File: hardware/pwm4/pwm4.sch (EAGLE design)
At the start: 79 parts, among them IC1 BSP75, IC2 PCA82C250SMD, IC3 BSP75, IC4 78L05SMD, IC6 BSP75, IC7 BSP75, Q1 18M432

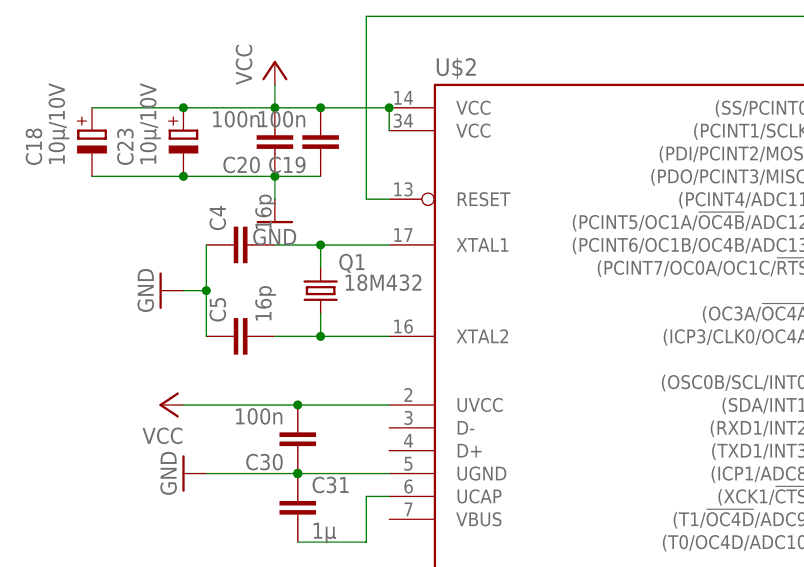
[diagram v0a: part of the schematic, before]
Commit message: changed crystal frequency
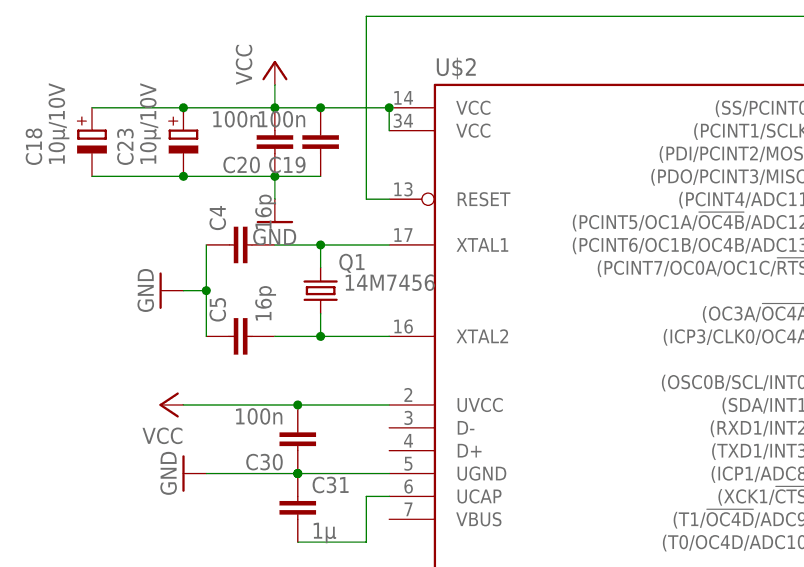
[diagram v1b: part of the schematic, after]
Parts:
- Q1: value 18M432 -> 14M7456
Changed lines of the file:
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@@
 <part name="C2" library="rcl" deviceset="CPOL-EU" device="A/3216-18W" value="10µ/10V"/>
 <part name="GND1" library="supply1" deviceset="GND" device=""/>
-<part name="Q1" library="crystal" deviceset="CRYSTAL" device="SM49" value="18M432"/>
+<part name="Q1" library="crystal" deviceset="CRYSTAL" device="SM49" value="14M7456"/>
 <part name="GND6" library="supply1" deviceset="GND" device=""/>
 <part name="C4" library="resistor" deviceset="C-EU" device="C0603" value="16p"/>

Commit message: optocoupler input and output resistor change
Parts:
- C22, C26, C6, C8: value 2n2 -> n.b.
- R1, R2, R3, R6: value 680 -> 1k2
- R10, R11, R7, R9: value 1k -> 2k2
- renumbered U$10 to BUS, U$5 to PWM0, U$6 to PWM1, U$7 to PWM2, U$8 to PWM3, U$9 to 24V
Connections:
- net N$33 renamed PWM1
- net N$34 renamed PWM2
- net N$35 renamed PWM0
- net N$5 renamed MOSI
- net N$6 renamed MISO
- net N$7 renamed SCK
- net N$8 renamed PWM3
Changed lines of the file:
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@@
 <part name="D15" library="diode" deviceset="SCHOTTKY-DIODE" device="SMD" value="SS24"/>
 <part name="U$4" library="mylib" deviceset="TCMT4100" device=""/>
-<part name="R1" library="resistor" deviceset="R-EU_" device="R0603" value="680"/>
-<part name="R2" library="resistor" deviceset="R-EU_" device="R0603" value="680"/>
-<part name="R3" library="resistor" deviceset="R-EU_" device="R0603" value="680"/>
-<part name="R6" library="resistor" deviceset="R-EU_" device="R0603" value="680"/>
+<part name="R1" library="resistor" deviceset="R-EU_" device="R0603" value="1k2"/>
+<part name="R2" library="resistor" deviceset="R-EU_" device="R0603" value="1k2"/>
+<part name="R3" library="resistor" deviceset="R-EU_" device="R0603" value="1k2"/>
+<part name="R6" library="resistor" deviceset="R-EU_" device="R0603" value="1k2"/>
 <part name="GND14" library="supply1" deviceset="GND" device=""/>
 <part name="GND15" library="supply1" deviceset="GND" device=""/>
@@
 <part name="VCC4" library="supply1" deviceset="VCCIO" device=""/>
 <part name="VCC5" library="supply1" deviceset="VCCIO" device=""/>
-<part name="R7" library="resistor" deviceset="R-EU_" device="R0603" value="1k"/>
-<part name="R9" library="resistor" deviceset="R-EU_" device="R0603" value="1k"/>
-<part name="R10" library="resistor" deviceset="R-EU_" device="R0603" value="1k"/>
-<part name="R11" library="resistor" deviceset="R-EU_" device="R0603" value="1k"/>
+<part name="R7" library="resistor" deviceset="R-EU_" device="R0603" value="2k2"/>
+<part name="R9" library="resistor" deviceset="R-EU_" device="R0603" value="2k2"/>
+<part name="R10" library="resistor" deviceset="R-EU_" device="R0603" value="2k2"/>
+<part name="R11" library="resistor" deviceset="R-EU_" device="R0603" value="2k2"/>
 <part name="GND20" library="supply1" deviceset="GNDIO" device=""/>
 <part name="GND21" library="supply1" deviceset="GNDIO" device=""/>
 <part name="GND28" library="supply1" deviceset="GNDIO" device=""/>
 <part name="GND29" library="supply1" deviceset="GNDIO" device=""/>
-<part name="U$5" library="mylib" deviceset="TBG-3.5-PW-2P" device=""/>
-<part name="U$6" library="mylib" deviceset="TBG-3.5-PW-2P" device=""/>
-<part name="U$7" library="mylib" deviceset="TBG-3.5-PW-2P" device=""/>
-<part name="U$8" library="mylib" deviceset="TBG-3.5-PW-2P" device=""/>
-<part name="U$9" library="mylib" deviceset="TBG-3.5-PW-2P" device=""/>
-<part name="U$10" library="mylib" deviceset="TBG-3.5-PW-4P" device=""/>
+<part name="PWM0" library="mylib" deviceset="TBG-3.5-PW-2P" device=""/>
+<part name="PWM1" library="mylib" deviceset="TBG-3.5-PW-2P" device=""/>
+<part name="PWM2" library="mylib" deviceset="TBG-3.5-PW-2P" device=""/>
+<part name="PWM3" library="mylib" deviceset="TBG-3.5-PW-2P" device=""/>
+<part name="24V" library="mylib" deviceset="TBG-3.5-PW-2P" device=""/>
+<part name="BUS" library="mylib" deviceset="TBG-3.5-PW-4P" device=""/>
 <part name="D11" library="diode" deviceset="SCHOTTKY-DIODE" device="SMC" value="SMCJ30A"/>
 <part name="U$2" library="mega32U4" deviceset="ATMEGA32U4-AU" device=""/>
-<part name="C6" library="resistor" deviceset="C-EU" device="025-040X050" value="2n2"/>
+<part name="C6" library="resistor" deviceset="C-EU" device="025-040X050" value="n.b."/>
 <part name="C7" library="resistor" deviceset="C-EU" device="025-040X050" value="2n2"/>
-<part name="C8" library="resistor" deviceset="C-EU" device="025-040X050" value="2n2"/>
+<part name="C8" library="resistor" deviceset="C-EU" device="025-040X050" value="n.b."/>
 <part name="C17" library="resistor" deviceset="C-EU" device="025-040X050" value="2n2"/>
-<part name="C22" library="resistor" deviceset="C-EU" device="025-040X050" value="2n2"/>
+<part name="C22" library="resistor" deviceset="C-EU" device="025-040X050" value="n.b."/>
 <part name="C24" library="resistor" deviceset="C-EU" device="025-040X050" value="2n2"/>
-<part name="C26" library="resistor" deviceset="C-EU" device="025-040X050" value="2n2"/>
+<part name="C26" library="resistor" deviceset="C-EU" device="025-040X050" value="n.b."/>
 <part name="C27" library="resistor" deviceset="C-EU" device="025-040X050" value="2n2"/>
 <part name="C28" library="resistor" deviceset="C-EU" device="025-040X050" value="2n2"/>
@@
 <instance part="GND28" gate="G$1" x="195.58" y="15.24"/>
 <instance part="GND29" gate="G$1" x="195.58" y="40.64"/>
-<instance part="U$5" gate="G$1" x="259.08" y="53.34" rot="R90"/>
-<instance part="U$6" gate="G$1" x="259.08" y="27.94" rot="R90"/>
-<instance part="U$7" gate="G$1" x="259.08" y="2.54" rot="R90"/>
-<instance part="U$8" gate="G$1" x="259.08" y="-22.86" rot="R90"/>
-<instance part="U$9" gate="G$1" x="248.92" y="-55.88" rot="R90"/>
-<instance part="U$10" gate="G$1" x="251.46" y="66.04" rot="R90"/>
+<instance part="PWM0" gate="G$1" x="259.08" y="53.34" rot="R90"/>
+<instance part="PWM1" gate="G$1" x="259.08" y="27.94" rot="R90"/>
+<instance part="PWM2" gate="G$1" x="259.08" y="2.54" rot="R90"/>
+<instance part="PWM3" gate="G$1" x="259.08" y="-22.86" rot="R90"/>
+<instance part="24V" gate="G$1" x="248.92" y="-55.88" rot="R90"/>
+<instance part="BUS" gate="G$1" x="251.46" y="66.04" rot="R90"/>
 <instance part="D11" gate="G$1" x="215.9" y="-50.8" rot="R90"/>
 <instance part="U$2" gate="G$1" x="53.34" y="78.74"/>
@@
 </busses>
 <nets>
-<net name="N$5" class="0">
+<net name="MOSI" class="0">
 <segment>
 <pinref part="U$1" gate="G$1" pin="MOSI"/>
@@
 </segment>
 </net>
-<net name="N$6" class="0">
+<net name="MISO" class="0">
 <segment>
 <pinref part="U$1" gate="G$1" pin="MISO"/>
@@
 </segment>
 </net>
-<net name="N$7" class="0">
+<net name="SCK" class="0">
 <segment>
 <pinref part="U$1" gate="G$1" pin="SCK"/>
@@
 <pinref part="GND5" gate="1" pin="GND"/>
 <wire x1="231.14" y1="71.12" x2="251.46" y2="71.12" width="0.1524" layer="91"/>
-<pinref part="U$10" gate="G$1" pin="2"/>
+<pinref part="BUS" gate="G$1" pin="2"/>
 </segment>
 <segment>
@@
 <pinref part="L4" gate="G$1" pin="4"/>
 <wire x1="238.76" y1="76.2" x2="251.46" y2="76.2" width="0.1524" layer="91"/>
-<pinref part="U$10" gate="G$1" pin="3"/>
+<pinref part="BUS" gate="G$1" pin="3"/>
 </segment>
 </net>
@@
 <pinref part="L4" gate="G$1" pin="3"/>
 <wire x1="238.76" y1="81.28" x2="251.46" y2="81.28" width="0.1524" layer="91"/>
-<pinref part="U$10" gate="G$1" pin="4"/>
+<pinref part="BUS" gate="G$1" pin="4"/>
 </segment>
 </net>
@@
 </segment>
 </net>
-<net name="N$8" class="0">
+<net name="PWM3" class="0">
 <segment>
 <wire x1="144.78" y1="50.8" x2="96.52" y2="50.8" width="0.1524" layer="91"/>
@@
 </segment>
 </net>
-<net name="N$33" class="0">
+<net name="PWM1" class="0">
 <segment>
 <wire x1="101.6" y1="55.88" x2="149.86" y2="55.88" width="0.1524" layer="91"/>
@@
 </segment>
 </net>
-<net name="N$34" class="0">
+<net name="PWM2" class="0">
 <segment>
 <pinref part="R3" gate="G$1" pin="2"/>
@@
 </segment>
 </net>
-<net name="N$35" class="0">
+<net name="PWM0" class="0">
 <segment>
 <wire x1="99.06" y1="58.42" x2="149.86" y2="58.42" width="0.1524" layer="91"/>
@@
 <wire x1="228.6" y1="53.34" x2="228.6" y2="55.88" width="0.1524" layer="91"/>
 <junction x="228.6" y="55.88"/>
-<pinref part="U$5" gate="G$1" pin="2"/>
+<pinref part="PWM0" gate="G$1" pin="2"/>
 <pinref part="C6" gate="G$1" pin="2"/>
 <junction x="243.84" y="55.88"/>
@@
 <wire x1="228.6" y1="27.94" x2="228.6" y2="30.48" width="0.1524" layer="91"/>
 <junction x="228.6" y="30.48"/>
-<pinref part="U$6" gate="G$1" pin="2"/>
+<pinref part="PWM1" gate="G$1" pin="2"/>
 <pinref part="C7" gate="G$1" pin="2"/>
 <junction x="236.22" y="30.48"/>
@@
 <wire x1="228.6" y1="2.54" x2="228.6" y2="5.08" width="0.1524" layer="91"/>
 <junction x="228.6" y="5.08"/>
-<pinref part="U$7" gate="G$1" pin="2"/>
+<pinref part="PWM2" gate="G$1" pin="2"/>
 <pinref part="C17" gate="G$1" pin="2"/>
 <junction x="236.22" y="5.08"/>
@@
 <wire x1="228.6" y1="-22.86" x2="228.6" y2="-20.32" width="0.1524" layer="91"/>
 <junction x="228.6" y="-20.32"/>
-<pinref part="U$8" gate="G$1" pin="2"/>
+<pinref part="PWM3" gate="G$1" pin="2"/>
 <pinref part="C24" gate="G$1" pin="2"/>
 <junction x="236.22" y="-20.32"/>
@@
 <wire x1="215.9" y1="-48.26" x2="215.9" y2="-40.64" width="0.1524" layer="91"/>
 <junction x="215.9" y="-40.64"/>
-<pinref part="U$5" gate="G$1" pin="1"/>
-<pinref part="U$6" gate="G$1" pin="1"/>
-<pinref part="U$7" gate="G$1" pin="1"/>
-<pinref part="U$8" gate="G$1" pin="1"/>
+<pinref part="PWM0" gate="G$1" pin="1"/>
+<pinref part="PWM1" gate="G$1" pin="1"/>
+<pinref part="PWM2" gate="G$1" pin="1"/>
+<pinref part="PWM3" gate="G$1" pin="1"/>
 <junction x="231.14" y="-40.64"/>
 <pinref part="D11" gate="G$1" pin="C"/>
@@
 <wire x1="246.38" y1="-58.42" x2="233.68" y2="-58.42" width="0.1524" layer="91"/>
 <pinref part="GND26" gate="G$1" pin="GNDIO"/>
-<pinref part="U$9" gate="G$1" pin="1"/>
+<pinref part="24V" gate="G$1" pin="1"/>
 </segment>
 <segment>
@@
 <pinref part="F1" gate="G$1" pin="2A"/>
 <wire x1="243.84" y1="-53.34" x2="246.38" y2="-53.34" width="0.1524" layer="91"/>
-<pinref part="U$9" gate="G$1" pin="2"/>
+<pinref part="24V" gate="G$1" pin="2"/>
 </segment>
 </net>
@@
 <wire x1="233.68" y1="129.54" x2="228.6" y2="129.54" width="0.1524" layer="91"/>
 <wire x1="246.38" y1="129.54" x2="246.38" y2="66.04" width="0.1524" layer="91"/>
-<pinref part="U$10" gate="G$1" pin="1"/>
+<pinref part="BUS" gate="G$1" pin="1"/>
 <wire x1="246.38" y1="66.04" x2="251.46" y2="66.04" width="0.1524" layer="91"/>
 <pinref part="D4" gate="G$1" pin="C"/>
